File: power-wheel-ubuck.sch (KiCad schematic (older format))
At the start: 0 parts

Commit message: Added initial symbol to schematic
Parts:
- added U?: TPS563200DDCR, *SOT-23-6*, symbol TPS563200DDCR
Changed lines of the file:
@@
 Comment4 ""
 $EndDescr
+$Comp
+L TPS563200DDCR U?
+U 1 1 59461737
+P 5500 3700
+F 0 "U?" H 5150 4150 60  0000 C CNN
+F 1 "TPS563200DDCR" H 5500 3700 30  0000 C CNN
+F 2 "*SOT-23-6*" H 5500 2650 60  0001 C CNN
+F 3 "http://www.ti.com/lit/ds/symlink/tps563200.pdf" H 5500 3000 60  0001 C CNN
+F 4 "TPS563200DDCR" H 5500 2850 60  0001 C CNN "MPN"
+F 5 "296-43663-1-ND" H 5500 2750 60  0001 C CNN "DKPN"
+	1    5500 3700
+	1    0    0    -1
+$EndComp
 $EndSCHEMATC

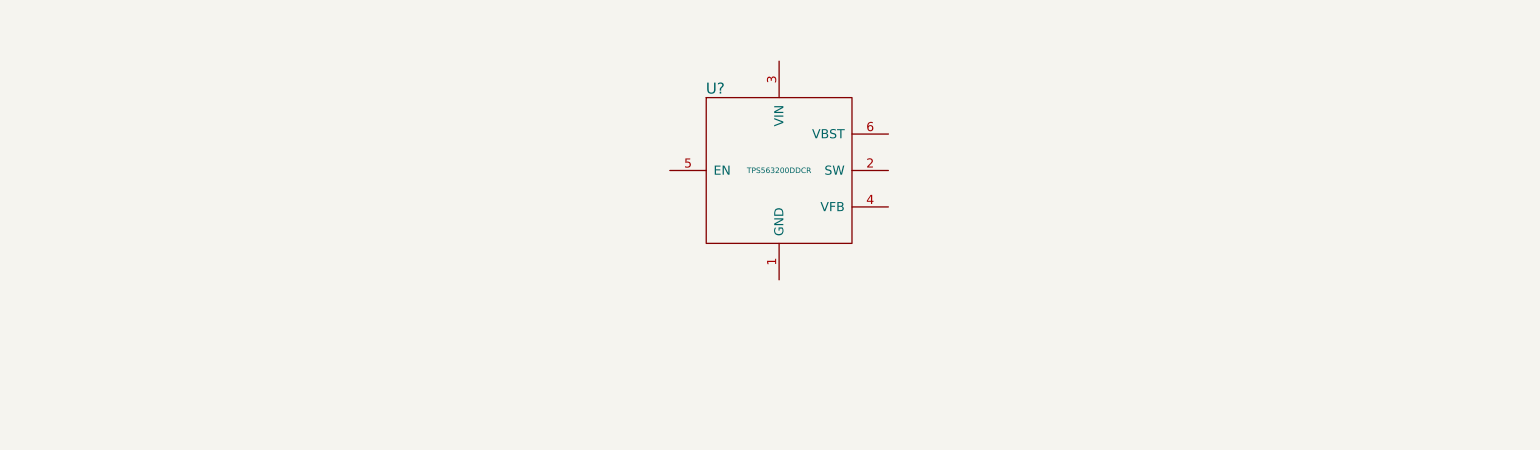
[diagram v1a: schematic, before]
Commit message: Schematic captured for initial run at board based on the TPS563200EVM-652 eval board
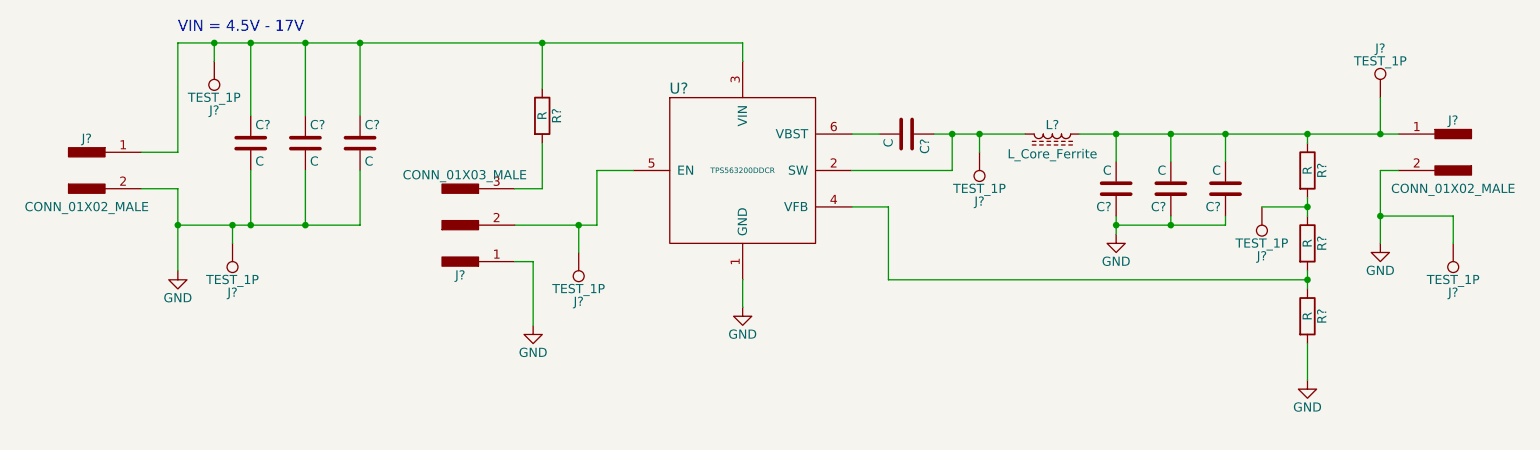
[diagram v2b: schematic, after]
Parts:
- added C? (x7): C, symbol C
- added J? (x2): CONN_01X02_MALE, symbol CONN_01X02_MALE
- added J? (x7): TEST_1P, symbol TEST_1P
- added J?: CONN_01X03_MALE, symbol CONN_01X03_MALE
- added L?: L_Core_Ferrite, symbol L_Core_Ferrite
- added R? (x4): R, symbol R
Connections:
- net GND: now reaches U?.1 (GND)
- net GND: now also C?.1, C?.1, C?.1, C?.2, C?.2, C?.2, J?.1, J?.1, J?.1, J?.2, J?.2, R?.2
- net at U?.2 (SW): now also C?.1, J?.1, L?.2
- net at U?.3 (VIN): now also C?.1, C?.1, C?.1, J?.1, J?.1, R?.1
- net at U?.4 (VFB): now also R?.1, R?.2
- net at U?.5 (EN): now also J?.1, J?.2
- net at U?.6 (VBST): now also C?.2
- new net: J?.3, R?.2
- new net: C?.2, C?.2, C?.2, J?.1, J?.1, L?.1, R?.1
- new net: J?.1, R?.1, R?.2
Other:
- note added: "VIN = 4.5V - 17V"
- moved on the sheet: U?

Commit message: Annotated parts and assigned values
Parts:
- C1, C4: renamed from C?; value C -> 0.1u
- C2, C3: renamed from C?; value C -> 10u
- C5, C6, C7: renamed from C?; value C -> 22u
- L1: renamed from L?; value L_Core_Ferrite -> 3.3u
- R1, R4: renamed from R?; value R -> 10K
- R2: renamed from R?; value R -> 0
- R3: renamed from R?; value R -> 54.9K
- gave numbers to parts that had none: 11
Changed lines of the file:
@@
 $EndDescr
 $Comp
-L TPS563200DDCR U?
+L TPS563200DDCR U1
 U 1 1 59461737
 P 5300 3700
-F 0 "U?" H 4950 4150 60  0000 C CNN
+F 0 "U1" H 4950 4150 60  0000 C CNN
 F 1 "TPS563200DDCR" H 5300 3700 30  0000 C CNN
 F 2 "*SOT-23-6*" H 5300 2650 60  0001 C CNN
@@
 $EndComp
 $Comp
-L CONN_01X02_MALE J?
+L CONN_01X02_MALE J1
 U 1 1 59461984
 P 1700 3700
-F 0 "J?" H 1700 3875 50  0000 C CNN
+F 0 "J1" H 1700 3875 50  0000 C CNN
 F 1 "CONN_01X02_MALE" H 1700 3500 50  0000 C CNN
 F 2 "" H 1700 3800 50  0001 C CNN
@@
 $EndComp
 $Comp
-L GND #PWR?
+L GND #PWR1
 U 1 1 594619D7
 P 2200 4250
-F 0 "#PWR?" H 2200 4000 50  0001 C CNN
+F 0 "#PWR1" H 2200 4000 50  0001 C CNN
 F 1 "GND" H 2200 4100 50  0000 C CNN
 F 2 "" H 2200 4250 50  0001 C CNN
@@
 VIN = 4.5V - 17V
 $Comp
-L C C?
+L C C1
 U 1 1 59461A32
 P 2600 3550
-F 0 "C?" H 2625 3650 50  0000 L CNN
-F 1 "C" H 2625 3450 50  0000 L CNN
+F 0 "C1" H 2625 3650 50  0000 L CNN
+F 1 "0.1u" H 2625 3450 50  0000 L CNN
 F 2 "" H 2638 3400 50  0001 C CNN
 F 3 "" H 2600 3550 50  0001 C CNN
@@
 $EndComp
 $Comp
-L C C?
+L C C2
 U 1 1 59461A72
 P 2900 3550
-F 0 "C?" H 2925 3650 50  0000 L CNN
-F 1 "C" H 2925 3450 50  0000 L CNN
+F 0 "C2" H 2925 3650 50  0000 L CNN
+F 1 "10u" H 2925 3450 50  0000 L CNN
 F 2 "" H 2938 3400 50  0001 C CNN
 F 3 "" H 2900 3550 50  0001 C CNN
@@
 $EndComp
 $Comp
-L C C?
+L C C3
 U 1 1 59461A9E
 P 3200 3550
-F 0 "C?" H 3225 3650 50  0000 L CNN
-F 1 "C" H 3225 3450 50  0000 L CNN
+F 0 "C3" H 3225 3650 50  0000 L CNN
+F 1 "10u" H 3225 3450 50  0000 L CNN
 F 2 "" H 3238 3400 50  0001 C CNN
 F 3 "" H 3200 3550 50  0001 C CNN
@@
 $EndComp
 $Comp
-L R R?
+L R R1
 U 1 1 59461AC4
 P 4200 3400
-F 0 "R?" V 4280 3400 50  0000 C CNN
-F 1 "R" V 4200 3400 50  0000 C CNN
+F 0 "R1" V 4280 3400 50  0000 C CNN
+F 1 "10K" V 4200 3400 50  0000 C CNN
 F 2 "" V 4130 3400 50  0001 C CNN
 F 3 "" H 4200 3400 50  0001 C CNN
@@
 $EndComp
 $Comp
-L TEST_1P J?
+L TEST_1P J2
 U 1 1 59461B0D
 P 2400 3100
-F 0 "J?" H 2400 3370 50  0000 C CNN
+F 0 "J2" H 2400 3370 50  0000 C CNN
 F 1 "TEST_1P" H 2400 3300 50  0000 C CNN
 F 2 "" H 2600 3100 50  0001 C CNN
@@
 Connection ~ 2400 3000
 $Comp
-L TEST_1P J?
+L TEST_1P J3
 U 1 1 59461BAA
 P 2500 4100
-F 0 "J?" H 2500 4370 50  0000 C CNN
+F 0 "J3" H 2500 4370 50  0000 C CNN
 F 1 "TEST_1P" H 2500 4300 50  0000 C CNN
 F 2 "" H 2700 4100 50  0001 C CNN
@@
 Connection ~ 2900 4000
 $Comp
-L CONN_01X03_MALE J?
+L CONN_01X03_MALE J4
 U 1 1 59461DE8
 P 3750 4000
-F 0 "J?" H 3750 4275 50  0000 C CNN
+F 0 "J4" H 3750 4275 50  0000 C CNN
 F 1 "CONN_01X03_MALE" H 3775 3725 50  0000 C CNN
 F 2 "" H 3750 4200 50  0001 C CNN
@@
 	4500 3700 4700 3700
 $Comp
-L TEST_1P J?
+L TEST_1P J5
 U 1 1 5946217B
 P 4400 4150
-F 0 "J?" H 4400 4420 50  0000 C CNN
+F 0 "J5" H 4400 4420 50  0000 C CNN
 F 1 "TEST_1P" H 4400 4350 50  0000 C CNN
 F 2 "" H 4600 4150 50  0001 C CNN
@@
 Connection ~ 4400 4000
 $Comp
-L GND #PWR?
+L GND #PWR2
 U 1 1 59462204
 P 4150 4550
-F 0 "#PWR?" H 4150 4300 50  0001 C CNN
+F 0 "#PWR2" H 4150 4300 50  0001 C CNN
 F 1 "GND" H 4150 4400 50  0000 C CNN
 F 2 "" H 4150 4550 50  0001 C CNN
@@
 	4150 4200 4150 4550
 $Comp
-L GND #PWR?
+L GND #PWR3
 U 1 1 5946225A
 P 5300 4450
-F 0 "#PWR?" H 5300 4200 50  0001 C CNN
+F 0 "#PWR3" H 5300 4200 50  0001 C CNN
 F 1 "GND" H 5300 4300 50  0000 C CNN
 F 2 "" H 5300 4450 50  0001 C CNN
@@
 $EndComp
 $Comp
-L C C?
+L C C4
 U 1 1 5946268D
 P 6200 3500
-F 0 "C?" H 6225 3600 50  0000 L CNN
-F 1 "C" H 6225 3400 50  0000 L CNN
+F 0 "C4" H 6225 3600 50  0000 L CNN
+F 1 "0.1u" H 6225 3400 50  0000 L CNN
 F 2 "" H 6238 3350 50  0001 C CNN
 F 3 "" H 6200 3500 50  0001 C CNN
@@
 	5900 3500 6050 3500
 $Comp
-L TEST_1P J?
+L TEST_1P J6
 U 1 1 59462719
 P 6600 3600
-F 0 "J?" H 6600 3870 50  0000 C CNN
+F 0 "J6" H 6600 3870 50  0000 C CNN
 F 1 "TEST_1P" H 6600 3800 50  0000 C CNN
 F 2 "" H 6800 3600 50  0001 C CNN
@@
 Connection ~ 6450 3500
 $Comp
-L L_Core_Ferrite L?
+L L_Core_Ferrite L1
 U 1 1 594627D5
 P 7000 3500
-F 0 "L?" V 6950 3500 50  0000 C CNN
-F 1 "L_Core_Ferrite" V 7110 3500 50  0000 C CNN
+F 0 "L1" V 6950 3500 50  0000 C CNN
+F 1 "3.3u" V 7110 3500 50  0000 C CNN
 F 2 "" H 7000 3500 50  0001 C CNN
 F 3 "" H 7000 3500 50  0001 C CNN
@@
 Connection ~ 6600 3500
 $Comp
-L GND #PWR?
+L GND #PWR4
 U 1 1 59462874
 P 7350 4050
-F 0 "#PWR?" H 7350 3800 50  0001 C CNN
+F 0 "#PWR4" H 7350 3800 50  0001 C CNN
 F 1 "GND" H 7350 3900 50  0000 C CNN
 F 2 "" H 7350 4050 50  0001 C CNN
@@
 	8800 3500 8900 3500
 $Comp
-L C C?
+L C C5
 U 1 1 594628EC
 P 7350 3800
-F 0 "C?" H 7375 3900 50  0000 L CNN
-F 1 "C" H 7375 3700 50  0000 L CNN
+F 0 "C5" H 7375 3900 50  0000 L CNN
+F 1 "22u" H 7375 3700 50  0000 L CNN
 F 2 "" H 7388 3650 50  0001 C CNN
 F 3 "" H 7350 3800 50  0001 C CNN
@@
 	7350 4000 7350 4050
 $Comp
-L C C?
+L C C6
 U 1 1 594629D0
 P 7650 3800
-F 0 "C?" H 7675 3900 50  0000 L CNN
-F 1 "C" H 7675 3700 50  0000 L CNN
+F 0 "C6" H 7675 3900 50  0000 L CNN
+F 1 "22u" H 7675 3700 50  0000 L CNN
 F 2 "" H 7688 3650 50  0001 C CNN
 F 3 "" H 7650 3800 50  0001 C CNN
@@
 $EndComp
 $Comp
-L C C?
+L C C7
 U 1 1 59462A15
 P 7950 3800
-F 0 "C?" H 7975 3900 50  0000 L CNN
-F 1 "C" H 7975 3700 50  0000 L CNN
+F 0 "C7" H 7975 3900 50  0000 L CNN
+F 1 "22u" H 7975 3700 50  0000 L CNN
 F 2 "" H 7988 3650 50  0001 C CNN
 F 3 "" H 7950 3800 50  0001 C CNN
@@
 Connection ~ 7650 4000
 $Comp
-L R R?
+L R R2
 U 1 1 59462CBC
 P 8400 3700
-F 0 "R?" V 8480 3700 50  0000 C CNN
-F 1 "R" V 8400 3700 50  0000 C CNN
+F 0 "R2" V 8480 3700 50  0000 C CNN
+F 1 "0" V 8400 3700 50  0000 C CNN
 F 2 "" V 8330 3700 50  0001 C CNN
 F 3 "" H 8400 3700 50  0001 C CNN
@@
 $EndComp
 $Comp
-L R R?
+L R R3
 U 1 1 59462E2D
 P 8400 4100
-F 0 "R?" V 8480 4100 50  0000 C CNN
-F 1 "R" V 8400 4100 50  0000 C CNN
+F 0 "R3" V 8480 4100 50  0000 C CNN
+F 1 "54.9K" V 8400 4100 50  0000 C CNN
 F 2 "" V 8330 4100 50  0001 C CNN
 F 3 "" H 8400 4100 50  0001 C CNN
@@
 $EndComp
 $Comp
-L R R?
+L R R4
 U 1 1 59462F5D
 P 8400 4500
-F 0 "R?" V 8480 4500 50  0000 C CNN
-F 1 "R" V 8400 4500 50  0000 C CNN
+F 0 "R4" V 8480 4500 50  0000 C CNN
+F 1 "10K" V 8400 4500 50  0000 C CNN
 F 2 "" V 8330 4500 50  0001 C CNN
 F 3 "" H 8400 4500 50  0001 C CNN
@@
 $EndComp
 $Comp
-L TEST_1P J?
+L TEST_1P J7
 U 1 1 594630AA
 P 8150 3900
-F 0 "J?" H 8150 4170 50  0000 C CNN
+F 0 "J7" H 8150 4170 50  0000 C CNN
 F 1 "TEST_1P" H 8150 4100 50  0000 C CNN
 F 2 "" H 8350 3900 50  0001 C CNN
@@
 $EndComp
 $Comp
-L GND #PWR?
+L GND #PWR5
 U 1 1 5946329C
 P 8400 4850
-F 0 "#PWR?" H 8400 4600 50  0001 C CNN
+F 0 "#PWR5" H 8400 4600 50  0001 C CNN
 F 1 "GND" H 8400 4700 50  0000 C CNN
 F 2 "" H 8400 4850 50  0001 C CNN
@@
 Connection ~ 8400 3900
 $Comp
-L CONN_01X02_MALE J?
+L CONN_01X02_MALE J9
 U 1 1 59463819
 P 9200 3600
-F 0 "J?" H 9200 3775 50  0000 C CNN
+F 0 "J9" H 9200 3775 50  0000 C CNN
 F 1 "CONN_01X02_MALE" H 9200 3400 50  0000 C CNN
 F 2 "" H 9200 3700 50  0001 C CNN
@@
 Connection ~ 8400 3500
 $Comp
-L TEST_1P J?
+L TEST_1P J8
 U 1 1 59464272
 P 8800 3300
-F 0 "J?" H 8800 3570 50  0000 C CNN
+F 0 "J8" H 8800 3570 50  0000 C CNN
 F 1 "TEST_1P" H 8800 3500 50  0000 C CNN
 F 2 "" H 9000 3300 50  0001 C CNN
@@
 Connection ~ 8800 3500
 $Comp
-L GND #PWR?
+L GND #PWR6
 U 1 1 59464349
 P 8800 4100
-F 0 "#PWR?" H 8800 3850 50  0001 C CNN
+F 0 "#PWR6" H 8800 3850 50  0001 C CNN
 F 1 "GND" H 8800 3950 50  0000 C CNN
 F 2 "" H 8800 4100 50  0001 C CNN
@@
 	8800 3950 8800 4100
 $Comp
-L TEST_1P J?
+L TEST_1P J10
 U 1 1 594643F3
 P 9200 4100
-F 0 "J?" H 9200 4370 50  0000 C CNN
+F 0 "J10" H 9200 4370 50  0000 C CNN
 F 1 "TEST_1P" H 9200 4300 50  0000 C CNN
 F 2 "" H 9400 4100 50  0001 C CNN

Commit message: Associated footprints with parts
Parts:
- C1, C2, C3, C4, C5, C6, C7: footprint (none) -> Capacitors_SMD:C_0805_HandSoldering
- J1, J9: footprint (none) -> Pin_Headers:Pin_Header_Straight_1x02_Pitch2.54mm
- J10, J2, J3, J5, J6, J7, J8: footprint (none) -> Measurement_Points:Measurement_Point_Square-SMD-Pad_Big
- J4: footprint (none) -> Pin_Headers:Pin_Header_Straight_1x03_Pitch2.54mm
- L1: footprint (none) -> power-wheel-ubuck-passives:VLS5045EX
- R1, R2, R3, R4: footprint (none) -> Resistors_SMD:R_0805_HandSoldering
- U1: footprint *SOT-23-6* -> TO_SOT_Packages_SMD:SOT-23-6_Handsoldering
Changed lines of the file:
@@
 F 0 "U1" H 4950 4150 60  0000 C CNN
 F 1 "TPS563200DDCR" H 5300 3700 30  0000 C CNN
-F 2 "*SOT-23-6*" H 5300 2650 60  0001 C CNN
+F 2 "TO_SOT_Packages_SMD:SOT-23-6_Handsoldering" H 5300 2650 60  0001 C CNN
 F 3 "http://www.ti.com/lit/ds/symlink/tps563200.pdf" H 5300 3000 60  0001 C CNN
 F 4 "TPS563200DDCR" H 5300 2850 60  0001 C CNN "MPN"
@@
 F 0 "J1" H 1700 3875 50  0000 C CNN
 F 1 "CONN_01X02_MALE" H 1700 3500 50  0000 C CNN
-F 2 "" H 1700 3800 50  0001 C CNN
+F 2 "Pin_Headers:Pin_Header_Straight_1x02_Pitch2.54mm" H 1700 3800 50  0001 C CNN
 F 3 "" H 1700 3800 50  0001 C CNN
 	1    1700 3700
@@
 $EndComp
 $Comp
-L GND #PWR1
+L GND #PWR01
 U 1 1 594619D7
 P 2200 4250
-F 0 "#PWR1" H 2200 4000 50  0001 C CNN
+F 0 "#PWR01" H 2200 4000 50  0001 C CNN
 F 1 "GND" H 2200 4100 50  0000 C CNN
 F 2 "" H 2200 4250 50  0001 C CNN
@@
 	2000 3800 2200 3800
 Wire Wire Line
-	2200 3800 2200 4000
-Wire Wire Line
-	2200 4000 2200 4250
+	2200 3800 2200 4250
 Wire Wire Line
 	2000 3600 2200 3600
@@
 	2200 3600 2200 3000
 Wire Wire Line
-	2200 3000 2400 3000
-Wire Wire Line
-	2400 3000 2600 3000
-Wire Wire Line
-	2600 3000 2900 3000
-Wire Wire Line
-	2900 3000 3200 3000
-Wire Wire Line
-	3200 3000 4200 3000
-Wire Wire Line
-	4200 3000 5300 3000
+	2200 3000 5300 3000
 Wire Wire Line
 	5300 3000 5300 3100
@@
 F 0 "C1" H 2625 3650 50  0000 L CNN
 F 1 "0.1u" H 2625 3450 50  0000 L CNN
-F 2 "" H 2638 3400 50  0001 C CNN
+F 2 "Capacitors_SMD:C_0805_HandSoldering" H 2638 3400 50  0001 C CNN
 F 3 "" H 2600 3550 50  0001 C CNN
 	1    2600 3550
@@
 F 0 "C2" H 2925 3650 50  0000 L CNN
 F 1 "10u" H 2925 3450 50  0000 L CNN
-F 2 "" H 2938 3400 50  0001 C CNN
+F 2 "Capacitors_SMD:C_0805_HandSoldering" H 2938 3400 50  0001 C CNN
 F 3 "" H 2900 3550 50  0001 C CNN
 	1    2900 3550
@@
 F 0 "C3" H 3225 3650 50  0000 L CNN
 F 1 "10u" H 3225 3450 50  0000 L CNN
-F 2 "" H 3238 3400 50  0001 C CNN
+F 2 "Capacitors_SMD:C_0805_HandSoldering" H 3238 3400 50  0001 C CNN
 F 3 "" H 3200 3550 50  0001 C CNN
 	1    3200 3550
@@
 F 0 "R1" V 4280 3400 50  0000 C CNN
 F 1 "10K" V 4200 3400 50  0000 C CNN
-F 2 "" V 4130 3400 50  0001 C CNN
+F 2 "Resistors_SMD:R_0805_HandSoldering" V 4130 3400 50  0001 C CNN
 F 3 "" H 4200 3400 50  0001 C CNN
 	1    4200 3400
@@
 F 0 "J2" H 2400 3370 50  0000 C CNN
 F 1 "TEST_1P" H 2400 3300 50  0000 C CNN
-F 2 "" H 2600 3100 50  0001 C CNN
+F 2 "Measurement_Points:Measurement_Point_Square-SMD-Pad_Big" H 2600 3100 50  0001 C CNN
 F 3 "" H 2600 3100 50  0001 C CNN
 	1    2400 3100
@@
 F 0 "J3" H 2500 4370 50  0000 C CNN
 F 1 "TEST_1P" H 2500 4300 50  0000 C CNN
-F 2 "" H 2700 4100 50  0001 C CNN
+F 2 "Measurement_Points:Measurement_Point_Square-SMD-Pad_Big" H 2700 4100 50  0001 C CNN
 F 3 "" H 2700 4100 50  0001 C CNN
 	1    2500 4100
@@
 	3200 4000 3200 3700
 Wire Wire Line
-	2200 4000 2500 4000
-Wire Wire Line
-	2500 4000 2600 4000
-Wire Wire Line
-	2600 4000 2900 4000
-Wire Wire Line
-	2900 4000 3200 4000
+	2200 4000 3200 4000
 Wire Wire Line
 	3200 3400 3200 3000
@@
 F 0 "J4" H 3750 4275 50  0000 C CNN
 F 1 "CONN_01X03_MALE" H 3775 3725 50  0000 C CNN
-F 2 "" H 3750 4200 50  0001 C CNN
+F 2 "Pin_Headers:Pin_Header_Straight_1x03_Pitch2.54mm" H 3750 4200 50  0001 C CNN
 F 3 "" H 3750 4200 50  0001 C CNN
 	1    3750 4000
@@
 Connection ~ 4200 3000
 Wire Wire Line
-	4050 4000 4400 4000
-Wire Wire Line
-	4400 4000 4500 4000
+	4050 4000 4500 4000
 Wire Wire Line
 	4500 4000 4500 3700
@@
 F 0 "J5" H 4400 4420 50  0000 C CNN
 F 1 "TEST_1P" H 4400 4350 50  0000 C CNN
-F 2 "" H 4600 4150 50  0001 C CNN
+F 2 "Measurement_Points:Measurement_Point_Square-SMD-Pad_Big" H 4600 4150 50  0001 C CNN
 F 3 "" H 4600 4150 50  0001 C CNN
 	1    4400 4150
@@
 Connection ~ 4400 4000
 $Comp
-L GND #PWR2
+L GND #PWR02
 U 1 1 59462204
 P 4150 4550
-F 0 "#PWR2" H 4150 4300 50  0001 C CNN
+F 0 "#PWR02" H 4150 4300 50  0001 C CNN
 F 1 "GND" H 4150 4400 50  0000 C CNN
 F 2 "" H 4150 4550 50  0001 C CNN
@@
 	4150 4200 4150 4550
 $Comp
-L GND #PWR3
+L GND #PWR03
 U 1 1 5946225A
 P 5300 4450
-F 0 "#PWR3" H 5300 4200 50  0001 C CNN
+F 0 "#PWR03" H 5300 4200 50  0001 C CNN
 F 1 "GND" H 5300 4300 50  0000 C CNN
 F 2 "" H 5300 4450 50  0001 C CNN
@@
 F 0 "C4" H 6225 3600 50  0000 L CNN
 F 1 "0.1u" H 6225 3400 50  0000 L CNN
-F 2 "" H 6238 3350 50  0001 C CNN
+F 2 "Capacitors_SMD:C_0805_HandSoldering" H 6238 3350 50  0001 C CNN
 F 3 "" H 6200 3500 50  0001 C CNN
 	1    6200 3500
@@
 F 0 "J6" H 6600 3870 50  0000 C CNN
 F 1 "TEST_1P" H 6600 3800 50  0000 C CNN
-F 2 "" H 6800 3600 50  0001 C CNN
+F 2 "Measurement_Points:Measurement_Point_Square-SMD-Pad_Big" H 6800 3600 50  0001 C CNN
 F 3 "" H 6800 3600 50  0001 C CNN
 	1    6600 3600
@@
 $EndComp
 Wire Wire Line
-	6600 3600 6600 3500
-Wire Wire Line
-	6350 3500 6450 3500
-Wire Wire Line
-	6450 3500 6600 3500
-Wire Wire Line
-	6600 3500 6850 3500
+	6600 3500 6600 3600
+Wire Wire Line
+	6350 3500 6850 3500
 Wire Wire Line
 	5900 3700 6450 3700
@@
 F 0 "L1" V 6950 3500 50  0000 C CNN
 F 1 "3.3u" V 7110 3500 50  0000 C CNN
-F 2 "" H 7000 3500 50  0001 C CNN
+F 2 "power-wheel-ubuck-passives:VLS5045EX" H 7000 3500 50  0001 C CNN
 F 3 "" H 7000 3500 50  0001 C CNN
 	1    7000 3500
@@
 Connection ~ 6600 3500
 $Comp
-L GND #PWR4
+L GND #PWR04
 U 1 1 59462874
 P 7350 4050
-F 0 "#PWR4" H 7350 3800 50  0001 C CNN
+F 0 "#PWR04" H 7350 3800 50  0001 C CNN
 F 1 "GND" H 7350 3900 50  0000 C CNN
 F 2 "" H 7350 4050 50  0001 C CNN
@@
 $EndComp
 Wire Wire Line
-	7150 3500 7350 3500
-Wire Wire Line
-	7350 3500 7650 3500
-Wire Wire Line
-	7650 3500 7950 3500
-Wire Wire Line
-	7950 3500 8400 3500
-Wire Wire Line
-	8400 3500 8800 3500
-Wire Wire Line
-	8800 3500 8900 3500
+	7150 3500 8900 3500
 $Comp
 L C C5
@@
 F 0 "C5" H 7375 3900 50  0000 L CNN
 F 1 "22u" H 7375 3700 50  0000 L CNN
-F 2 "" H 7388 3650 50  0001 C CNN
+F 2 "Capacitors_SMD:C_0805_HandSoldering" H 7388 3650 50  0001 C CNN
 F 3 "" H 7350 3800 50  0001 C CNN
 	1    7350 3800
@@
 	7350 3500 7350 3650
 Wire Wire Line
-	7350 3950 7350 4000
-Wire Wire Line
-	7350 4000 7350 4050
+	7350 3950 7350 4050
 $Comp
 L C C6
@@
 F 0 "C6" H 7675 3900 50  0000 L CNN
 F 1 "22u" H 7675 3700 50  0000 L CNN
-F 2 "" H 7688 3650 50  0001 C CNN
+F 2 "Capacitors_SMD:C_0805_HandSoldering" H 7688 3650 50  0001 C CNN
 F 3 "" H 7650 3800 50  0001 C CNN
 	1    7650 3800
@@
 F 0 "C7" H 7975 3900 50  0000 L CNN
 F 1 "22u" H 7975 3700 50  0000 L CNN
-F 2 "" H 7988 3650 50  0001 C CNN
+F 2 "Capacitors_SMD:C_0805_HandSoldering" H 7988 3650 50  0001 C CNN
 F 3 "" H 7950 3800 50  0001 C CNN
 	1    7950 3800
@@
 	7650 3950 7650 4000
 Wire Wire Line
-	7350 4000 7650 4000
-Wire Wire Line
-	7650 4000 7950 4000
+	7350 4000 7950 4000
 Connection ~ 7350 4000
 Wire Wire Line
@@
 F 0 "R2" V 8480 3700 50  0000 C CNN
 F 1 "0" V 8400 3700 50  0000 C CNN
-F 2 "" V 8330 3700 50  0001 C CNN
+F 2 "Resistors_SMD:R_0805_HandSoldering" V 8330 3700 50  0001 C CNN
 F 3 "" H 8400 3700 50  0001 C CNN
 	1    8400 3700
@@
 F 0 "R3" V 8480 4100 50  0000 C CNN
 F 1 "54.9K" V 8400 4100 50  0000 C CNN
-F 2 "" V 8330 4100 50  0001 C CNN
+F 2 "Resistors_SMD:R_0805_HandSoldering" V 8330 4100 50  0001 C CNN
 F 3 "" H 8400 4100 50  0001 C CNN
 	1    8400 4100
@@
 F 0 "R4" V 8480 4500 50  0000 C CNN
 F 1 "10K" V 8400 4500 50  0000 C CNN
-F 2 "" V 8330 4500 50  0001 C CNN
+F 2 "Resistors_SMD:R_0805_HandSoldering" V 8330 4500 50  0001 C CNN
 F 3 "" H 8400 4500 50  0001 C CNN
 	1    8400 4500
@@
 F 0 "J7" H 8150 4170 50  0000 C CNN
 F 1 "TEST_1P" H 8150 4100 50  0000 C CNN
-F 2 "" H 8350 3900 50  0001 C CNN
+F 2 "Measurement_Points:Measurement_Point_Square-SMD-Pad_Big" H 8350 3900 50  0001 C CNN
 F 3 "" H 8350 3900 50  0001 C CNN
 	1    8150 3900
@@
 $EndComp
 $Comp
-L GND #PWR5
+L GND #PWR05
 U 1 1 5946329C
 P 8400 4850
-F 0 "#PWR5" H 8400 4600 50  0001 C CNN
+F 0 "#PWR05" H 8400 4600 50  0001 C CNN
 F 1 "GND" H 8400 4700 50  0000 C CNN
 F 2 "" H 8400 4850 50  0001 C CNN
@@
 	6100 4300 8400 4300
 Wire Wire Line
-	8400 4250 8400 4300
-Wire Wire Line
-	8400 4300 8400 4350
+	8400 4250 8400 4350
 Wire Wire Line
 	8400 3500 8400 3550
 Connection ~ 7950 3500
 Wire Wire Line
-	8400 3850 8400 3900
-Wire Wire Line
-	8400 3900 8400 3950
+	8400 3850 8400 3950
 Connection ~ 8400 4300
 Wire Wire Line
@@
 F 0 "J9" H 9200 3775 50  0000 C CNN
 F 1 "CONN_01X02_MALE" H 9200 3400 50  0000 C CNN
-F 2 "" H 9200 3700 50  0001 C CNN
+F 2 "Pin_Headers:Pin_Header_Straight_1x02_Pitch2.54mm" H 9200 3700 50  0001 C CNN
 F 3 "" H 9200 3700 50  0001 C CNN
 	1    9200 3600
@@
 F 0 "J8" H 8800 3570 50  0000 C CNN
 F 1 "TEST_1P" H 8800 3500 50  0000 C CNN
-F 2 "" H 9000 3300 50  0001 C CNN
+F 2 "Measurement_Points:Measurement_Point_Square-SMD-Pad_Big" H 9000 3300 50  0001 C CNN
 F 3 "" H 9000 3300 50  0001 C CNN
 	1    8800 3300
@@
 Connection ~ 8800 3500
 $Comp
-L GND #PWR6
+L GND #PWR06
 U 1 1 59464349
 P 8800 4100
-F 0 "#PWR6" H 8800 3850 50  0001 C CNN
+F 0 "#PWR06" H 8800 3850 50  0001 C CNN
 F 1 "GND" H 8800 3950 50  0000 C CNN
 F 2 "" H 8800 4100 50  0001 C CNN
@@
 	8900 3700 8800 3700
 Wire Wire Line
-	8800 3700 8800 3950
-Wire Wire Line
-	8800 3950 8800 4100
+	8800 3700 8800 4100
 $Comp
 L TEST_1P J10
@@
 F 0 "J10" H 9200 4370 50  0000 C CNN
 F 1 "TEST_1P" H 9200 4300 50  0000 C CNN
-F 2 "" H 9400 4100 50  0001 C CNN
+F 2 "Measurement_Points:Measurement_Point_Square-SMD-Pad_Big" H 9400 4100 50  0001 C CNN
 F 3 "" H 9400 4100 50  0001 C CNN
 	1    9200 4100
